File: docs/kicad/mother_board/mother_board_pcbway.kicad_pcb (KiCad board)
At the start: 2 copper layers, 148 x 92.5 mm, 32 parts, among them J1 ROW_BOARDS, J10 PEDAL1, J11 PEDAL2, J12 PEDAL3, J13 PEDAL4, J14 GUITAR_IN, J15 LINE_OUT, J16 LEDS, J2 ROTARIES, J3 TE_DISPLAY, J4 RPI_DISPLAY, J5 rPi_5V, J6 RPI_RUN, J7 rpi_connector, J8 I2S_TXB, J9 EigthInchJack1, Q1 BC547, U1 teensyAudioRevD_WithAudio, U2 myTeensy4.1

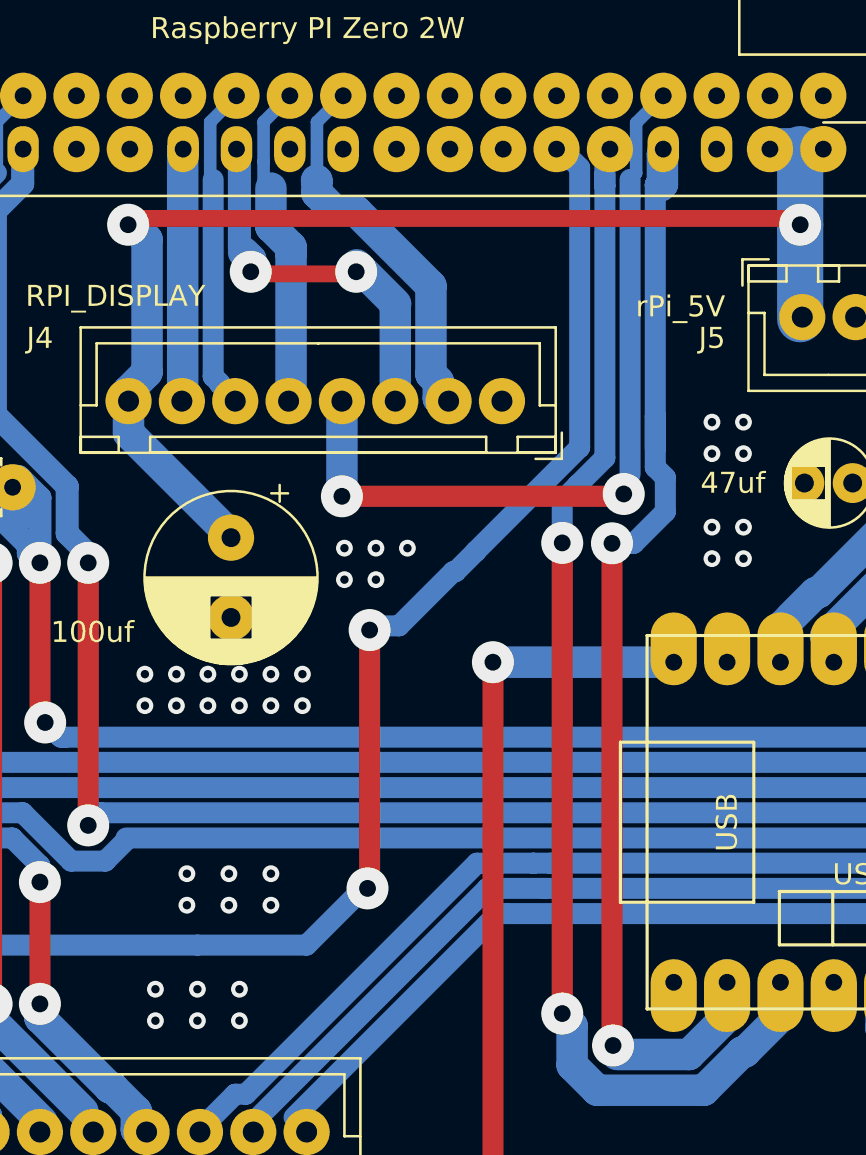
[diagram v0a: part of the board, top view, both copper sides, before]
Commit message: updated PCBWay designs after DRC Design Rules Checks
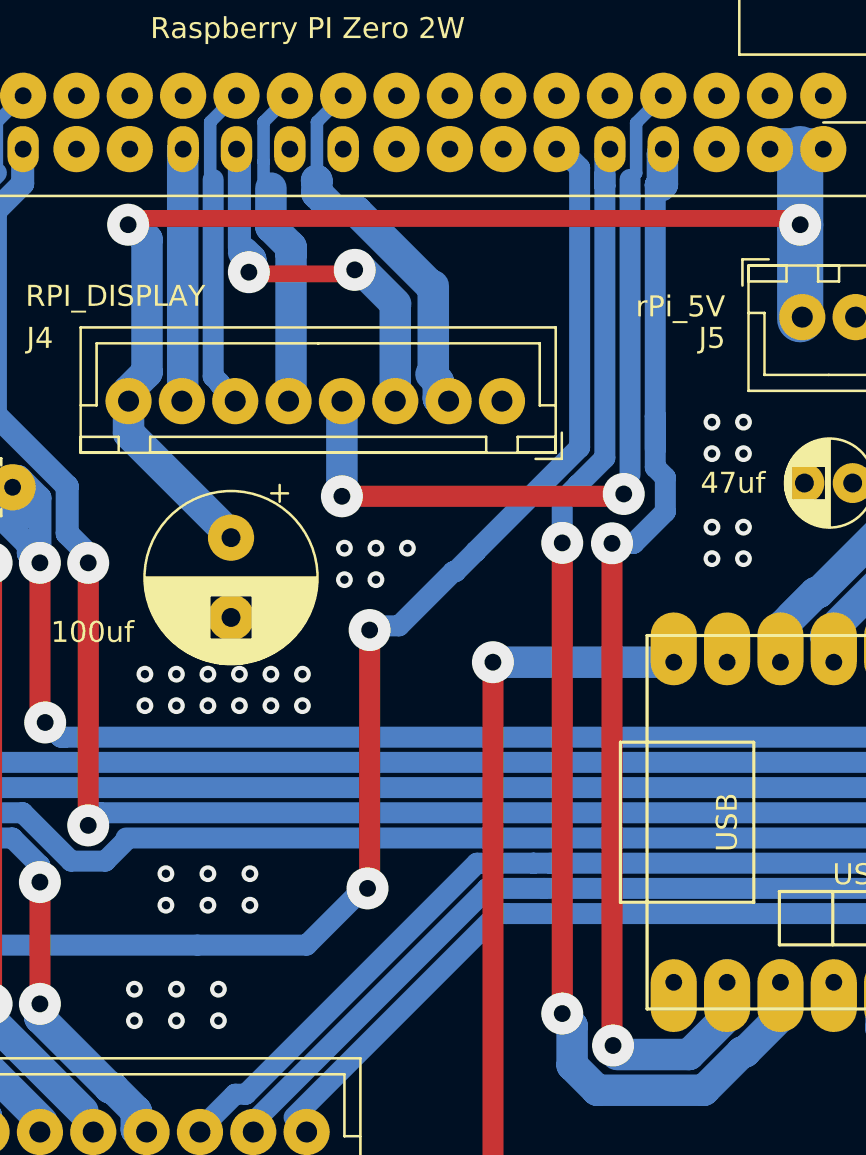
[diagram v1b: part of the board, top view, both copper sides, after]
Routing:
- net GND: vias 221 -> 233
- net (no net): vias 12 -> 0
